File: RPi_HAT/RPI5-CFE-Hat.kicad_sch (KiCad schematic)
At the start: 55 parts, among them J1 Conn_01x16_Shielded, J2 SFP, J3 Bus_M.2_Socket_M, J5 Conn_02x03_Odd_Even, U1 TPS564242DRLR, U2 PCA9306, U3 LM1117MP-1.8

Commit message: RPi5 HAT
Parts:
- added Q1, Q2, Q3: DMG1012T, Package_TO_SOT_SMD:SOT-523, symbol Transistor_FET:DMG1012T
- added R20, R21: NC, Resistor_SMD:R_0402_1005Metric_Pad0.72x0.64mm_HandSolder, symbol Device:R
- added R22: 33, Resistor_SMD:R_0402_1005Metric_Pad0.72x0.64mm_HandSolder, symbol Device:R
- added R23: 3k6, Resistor_SMD:R_0402_1005Metric_Pad0.72x0.64mm_HandSolder, symbol Device:R
- added R24, R25: 6k8, Resistor_SMD:R_0402_1005Metric_Pad0.72x0.64mm_HandSolder, symbol Device:R
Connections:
- net +3V3: now also Q1.1 (G), R20.2, R25.1; no longer TP5.1
- net +5V: now also R23.1
- net GND: now also Q2.2 (S), Q3.2 (S), R21.2, R24.2
- net PCIE_DET_WAKE: now also Q2.3 (D), R23.2, R24.1
- net PCIe_CLK_REQ: now also J3.52 (~{CLKREQ}), TP8.1
- net PCIe_RST: now also R22.1
- net PCIE_RST_SW: now reaches J3.50 (~{PERST}), R12.2, TP4.1
- net PCIE_RST_SW: now also Q1.2 (S), R20.1
- net PCIE_PEWAKE_N: now reaches J3.54 (~{PEWAKE}), R11.1
- net PCIE_PEWAKE_N: now also TP5.1, Q3.1 (G), R21.1
- new net: Q1.3 (D), R22.2
- new net: Q2.1 (G), Q3.3 (D), R25.2
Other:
- moved on the sheet: R11, R12, TP4, TP5, TP6, TP7, TP8

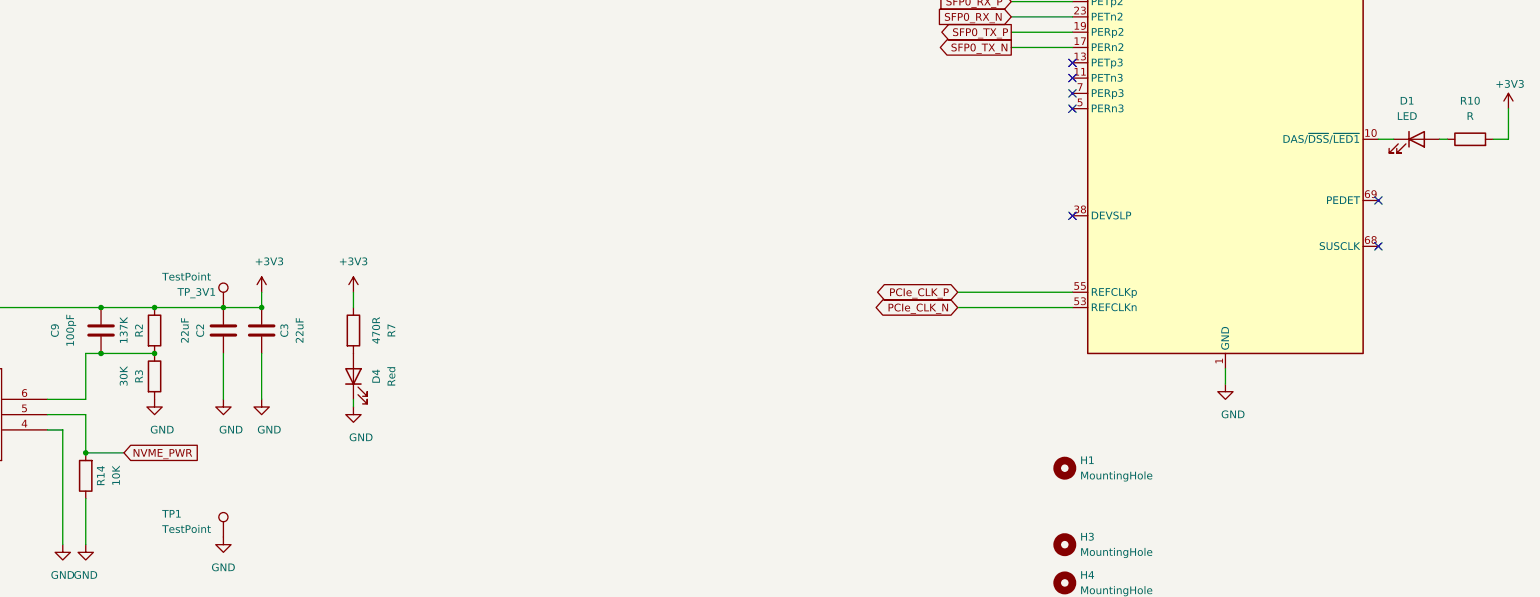
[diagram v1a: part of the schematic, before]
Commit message: cleanup BOM and generate inteactive BOM
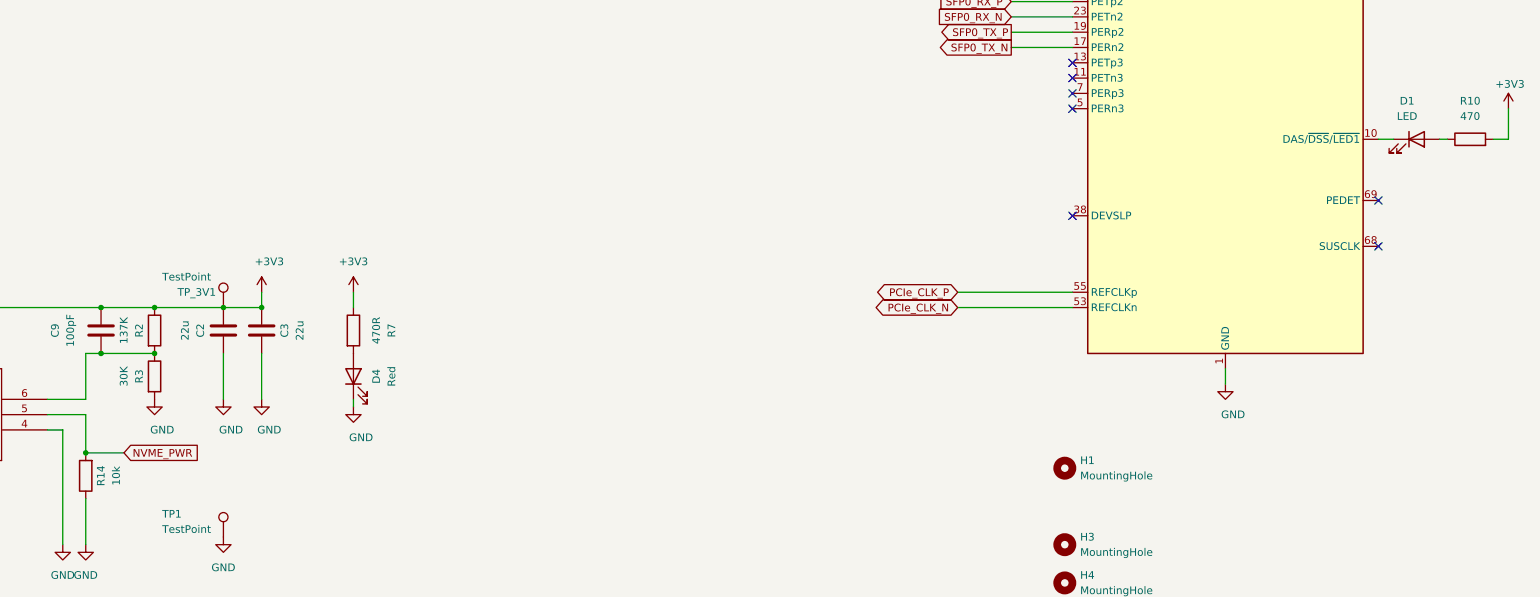
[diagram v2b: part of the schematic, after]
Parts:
- C2, C3: value 22uF -> 22u
- R10: value R -> 470
- R14: value 10K -> 10k
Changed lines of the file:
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@@
 			)
 		)
-		(property "Value" "R"
+		(property "Value" "470"
 			(at 326.39 190.5 90)
 			(effects
@@
 			)
 		)
-		(property "Value" "10K"
+		(property "Value" "10k"
 			(at 101.6 250.19 90)
 			(effects
@@
 			)
 		)
-		(property "Value" "22uF"
+		(property "Value" "22u"
 			(at 132.08 226.06 90)
 			(effects
@@
 			)
 		)
-		(property "Value" "22uF"
+		(property "Value" "22u"
 			(at 113.03 226.06 90)
 			(effects
